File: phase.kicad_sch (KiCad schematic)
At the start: 20 parts, among them J13 Conn_Coaxial, Q1 2N7002, Q2 2N7002, U1 MS5351, U15 74LVC74, Y1 25..27Mhz

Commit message: finich IF_RX_Schematics, begin MCU, delete *.sch files
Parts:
- removed C14, C3: 100nF, Capacitors_SMD:C_0603_HandSoldering, symbol C_Small
- removed C2: 10uF, LCSDR:CP_Radial_D5.0mm_P2.00mm, symbol CP_Small
- removed J13: Conn_Coaxial, LCSDR:U.FL_Molex_MCRF_73412-0110_Vertical, symbol Conn_Coaxial
- removed L10, L2: 100uH, Inductors_THT:L_Axial_L5.3mm_D2.2mm_P7.62mm_Horizontal_Vishay_IM-1, symbol L_Small
- removed Q1, Q2: 2N7002, TO_SOT_Packages_SMD:SOT-23, symbol 2N7002
- removed R15: 200R*, Resistors_SMD:R_0603_HandSoldering, symbol R_Small
- removed R5, R6, R7, R8: 6.8k, Resistors_SMD:R_0603_HandSoldering, symbol R_Small
- removed R56: 68, Resistors_SMD:R_0603_HandSoldering, symbol R_Small
- removed R57, R58, R59: 68, symbol R_Small
- removed U1: MS5351, LCSDR:MSOP-10_3x3mm_Pitch0.5mm, symbol SI5351
- removed U15: 74LVC74, Housings_SSOP:TSSOP-14_4.4x5mm_Pitch0.65mm, symbol 74HC74
- removed Y1: 25..27Mhz, Crystals:Crystal_HC49-U_Vertical, symbol Crystal
- added U7: 74HC74, symbol 74xx:74HC74
- added U8: Si5351A-B-GT, Package_SO:MSOP-10_3x3mm_P0.5mm, symbol Oscillator:Si5351A-B-GT

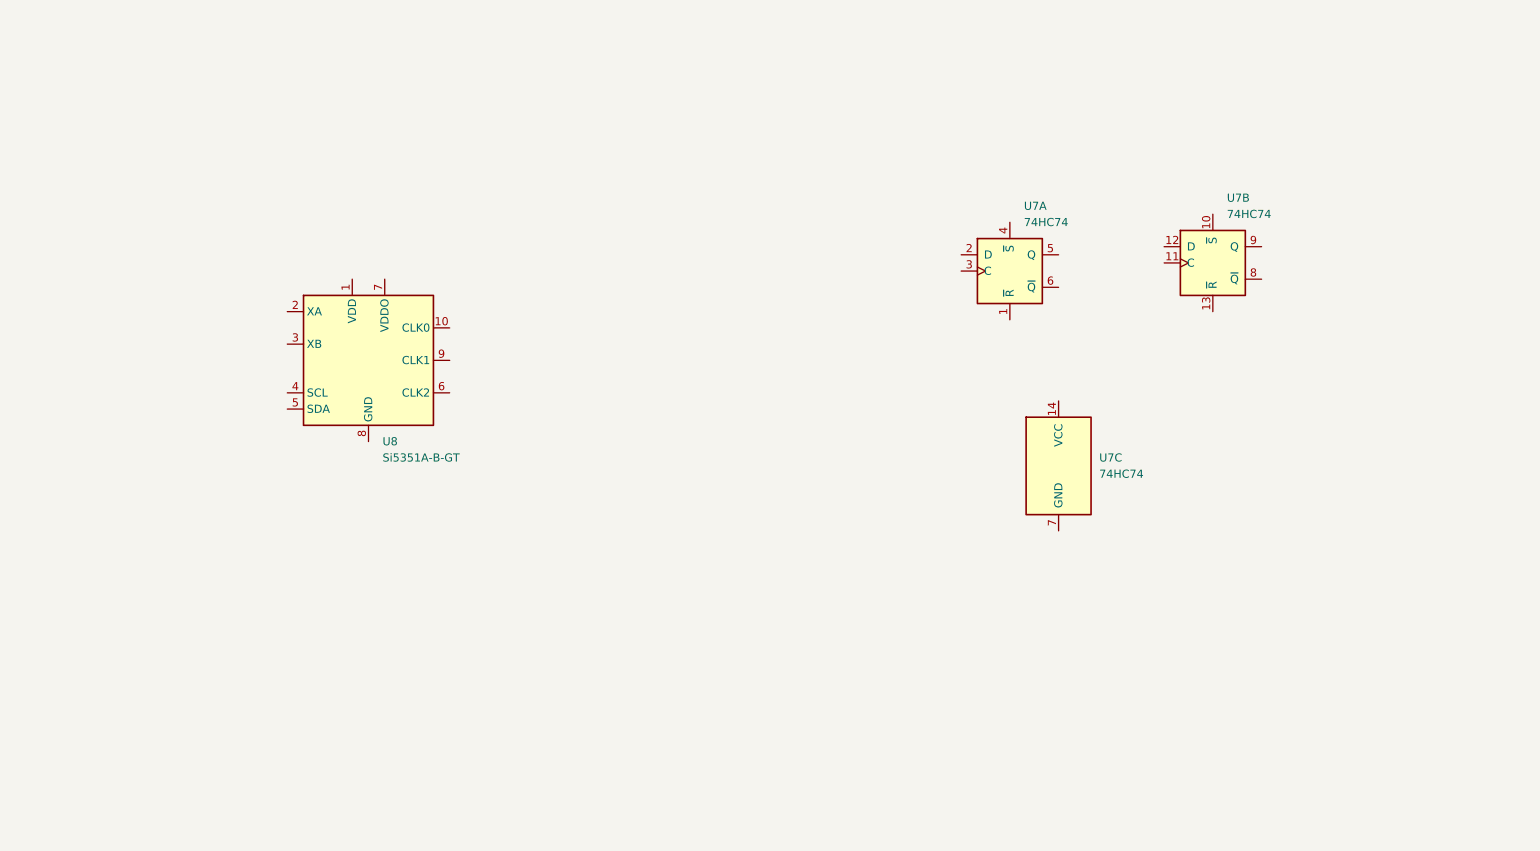
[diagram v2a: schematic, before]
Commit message: add custom footprints, progress on schema and PCB
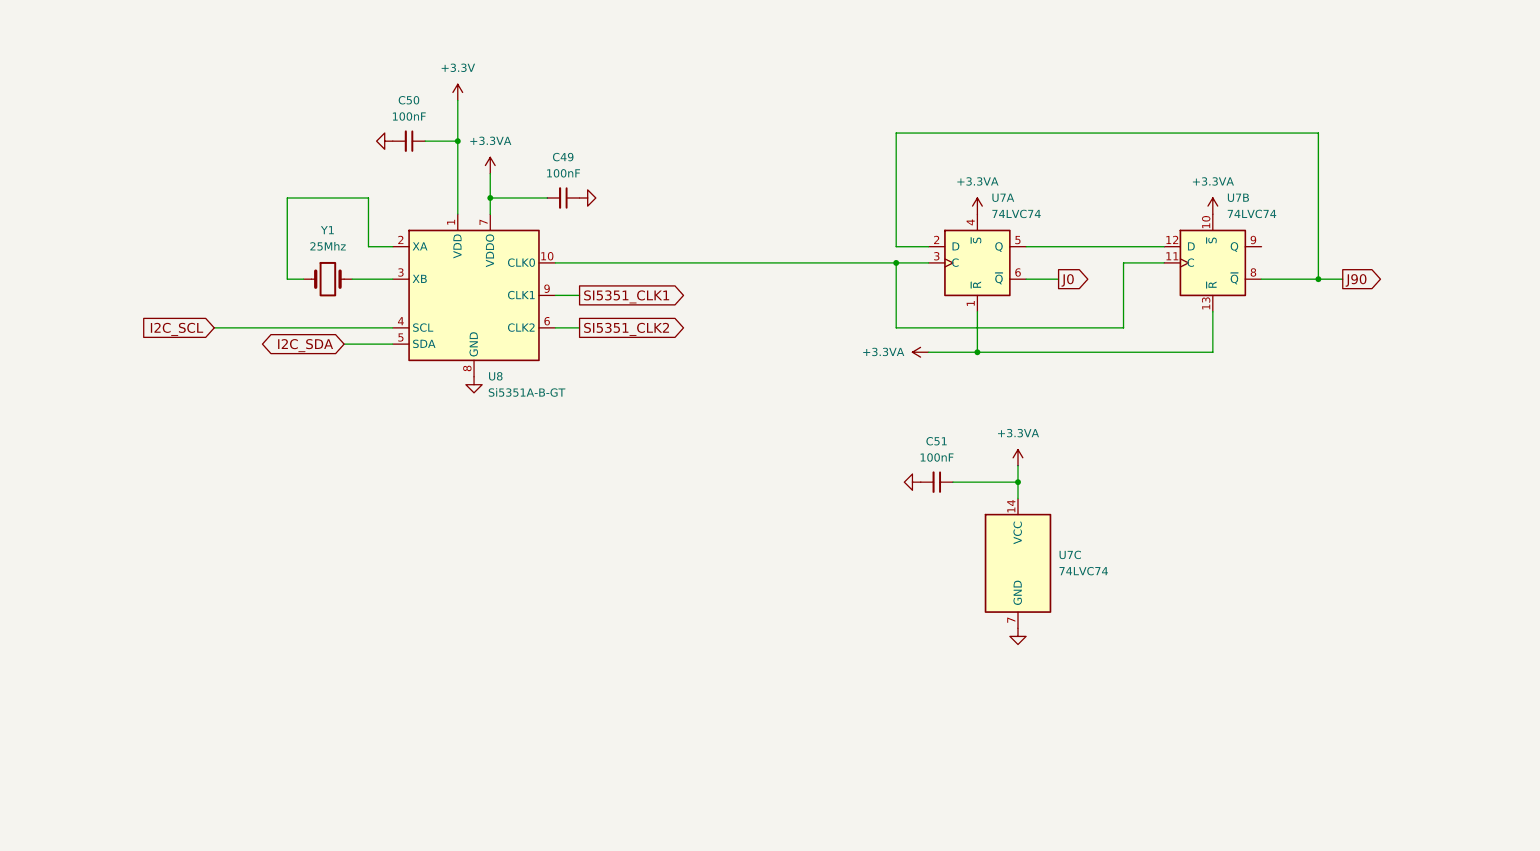
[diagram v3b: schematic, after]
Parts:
- added C49, C50, C51: 100nF, SDR_footprints:C_1206_0603, symbol Device:C_Small
- added Y1: 25Mhz, Crystal:Crystal_HC49-U_Vertical, symbol Device:Crystal
- U7: value 74HC74 -> 74LVC74; footprint (none) -> Package_SO:TSSOP-14_4.4x5mm_P0.65mm
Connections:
- net +3.3VA: now reaches U7.1 (~{R})
- net +3.3VA: now also U7.10 (~{S}), U7.13 (~{R}), U7.14 (VCC), U7.4 (~{S}), U8.7 (VDDO), C49.2, C51.1
- net J90: now reaches U7.2 (D)
- net J90: now also U7.8 (~{Q})
- net at U7.3 (C): now also U7.11 (C), U8.10 (CLK0)
- net at U7.5 (Q): now also U7.12 (D)
- net J0: now reaches U7.6 (~{Q})
- net GND: now reaches U7.7 (GND)
- net GND: now also U8.8 (GND), C49.1, C50.2, C51.2
- net +3.3V: now reaches U8.1 (VDD)
- net +3.3V: now also C50.1
- net at U8.2 (XA): now also Y1.1
- net at U8.3 (XB): now also Y1.2
- net I2C_SCL: now reaches U8.4 (SCL)
- net I2C_SDA: now reaches U8.5 (SDA)
- net SI5351_CLK2: now reaches U8.6 (CLK2)
- net SI5351_CLK1: now reaches U8.9 (CLK1)
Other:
- moved on the sheet: U7A, U7C, U8

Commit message: progress on PCB
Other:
- moved on the sheet: C49, C50, C51, U7A, U7B, U7C, U8, Y1
